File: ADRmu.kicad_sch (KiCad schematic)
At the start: 7 parts, among them J1 DIN41612_02x16_AC_EvenPins, J2 Conn_01x01, J3 Conn_01x01, J4 Conn_01x01, J5 Conn_01x01, J6 Conn_01x01, J7 Conn_01x01

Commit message: asdf
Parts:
- J2: value Conn_01x01 -> 10Vf
- J3: value Conn_01x01 -> 10Vs
- J4: value Conn_01x01 -> ADRf
- J5: value Conn_01x01 -> ADRs
- J6: value Conn_01x01 -> return
- J7: value Conn_01x01 -> guard
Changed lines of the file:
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@@
     (in_bom yes) (on_board yes) (fields_autoplaced)
     (property "Reference" "J4" (id 0) (at 236.22 80.01 0))
-    (property "Value" "Conn_01x01" (id 1) (at 236.22 82.55 0))
+    (property "Value" "ADRf" (id 1) (at 236.22 82.55 0))
     (property "Footprint" "Connector_Wire:SolderWire-1sqmm_1x01_D1.4mm_OD3.9mm" (id 2) (at 236.22 86.36 0)
       (effects (font (size 1.27 1.27)) hide)
@@
     (in_bom yes) (on_board yes) (fields_autoplaced)
     (property "Reference" "J6" (id 0) (at 236.22 110.49 0))
-    (property "Value" "Conn_01x01" (id 1) (at 236.22 113.03 0))
+    (property "Value" "return" (id 1) (at 236.22 113.03 0))
     (property "Footprint" "Connector_Wire:SolderWire-1sqmm_1x01_D1.4mm_OD3.9mm" (id 2) (at 236.22 116.84 0)
       (effects (font (size 1.27 1.27)) hide)
@@
     (in_bom yes) (on_board yes) (fields_autoplaced)
     (property "Reference" "J3" (id 0) (at 236.22 64.77 0))
-    (property "Value" "Conn_01x01" (id 1) (at 236.22 67.31 0))
+    (property "Value" "10Vs" (id 1) (at 236.22 67.31 0))
     (property "Footprint" "Connector_Wire:SolderWire-1sqmm_1x01_D1.4mm_OD3.9mm" (id 2) (at 236.22 71.12 0)
       (effects (font (size 1.27 1.27)) hide)
@@
     (in_bom yes) (on_board yes) (fields_autoplaced)
     (property "Reference" "J5" (id 0) (at 236.22 95.25 0))
-    (property "Value" "Conn_01x01" (id 1) (at 236.22 97.79 0))
+    (property "Value" "ADRs" (id 1) (at 236.22 97.79 0))
     (property "Footprint" "Connector_Wire:SolderWire-1sqmm_1x01_D1.4mm_OD3.9mm" (id 2) (at 236.22 101.6 0)
       (effects (font (size 1.27 1.27)) hide)
@@
     (in_bom yes) (on_board yes)
     (property "Reference" "J2" (id 0) (at 236.22 49.53 0))
-    (property "Value" "Conn_01x01" (id 1) (at 236.22 52.07 0))
+    (property "Value" "10Vf" (id 1) (at 236.22 52.07 0))
     (property "Footprint" "Connector_Wire:SolderWire-1sqmm_1x01_D1.4mm_OD3.9mm" (id 2) (at 236.22 55.88 0)
       (effects (font (size 1.27 1.27)) hide)
@@
     (in_bom yes) (on_board yes) (fields_autoplaced)
     (property "Reference" "J7" (id 0) (at 236.22 125.73 0))
-    (property "Value" "Conn_01x01" (id 1) (at 236.22 128.27 0))
+    (property "Value" "guard" (id 1) (at 236.22 128.27 0))
     (property "Footprint" "Connector_Wire:SolderWire-1sqmm_1x01_D1.4mm_OD3.9mm" (id 2) (at 236.22 132.08 0)
       (effects (font (size 1.27 1.27)) hide)
@@
       (reference "C12") (unit 1) (value "22u") (footprint "Capacitor_SMD:C_1206_3216Metric")
     )
+    (path "/027929a1-62dd-40f4-83d4-39d0de3b1543/6845caeb-6485-48fb-9c50-6cb716fb69d9"
+      (reference "C13") (unit 1) (value "100n") (footprint "Capacitor_SMD:C_0805_2012Metric")
+    )
     (path "/b2eac6f7-6f2b-41aa-9eec-9c2e749d1013/24683382-393e-4151-a76d-4bae24fbeada"
       (reference "C14") (unit 1) (value "100n") (footprint "Capacitor_SMD:C_0805_2012Metric")
@@
       (reference "D7") (unit 1) (value "D_Schottky") (footprint "Diode_SMD:D_SOD-123F")
     )
+    (path "/b2eac6f7-6f2b-41aa-9eec-9c2e749d1013/27618427-173e-42f1-8841-5bc123d4d738"
+      (reference "D8") (unit 1) (value "LED") (footprint "LED_SMD:LED_1206_3216Metric")
+    )
     (path "/b2eac6f7-6f2b-41aa-9eec-9c2e749d1013/8a7e1f15-efce-479e-b3d6-f978918d3a7f"
       (reference "H1") (unit 1) (value "MountingHole") (footprint "MountingHole:MountingHole_4.3mm_M4")
@@
     )
     (path "/adbf8438-12a3-4949-9d6c-a3b68a6378f0"
-      (reference "J2") (unit 1) (value "Conn_01x01") (footprint "Connector_Wire:SolderWire-1sqmm_1x01_D1.4mm_OD3.9mm")
+      (reference "J2") (unit 1) (value "10Vf") (footprint "Connector_Wire:SolderWire-1sqmm_1x01_D1.4mm_OD3.9mm")
     )
     (path "/4bee5892-6b3a-433a-b771-068c80bdc6e8"
-      (reference "J3") (unit 1) (value "Conn_01x01") (footprint "Connector_Wire:SolderWire-1sqmm_1x01_D1.4mm_OD3.9mm")
+      (reference "J3") (unit 1) (value "10Vs") (footprint "Connector_Wire:SolderWire-1sqmm_1x01_D1.4mm_OD3.9mm")
     )
     (path "/27299abf-eabb-45db-a109-6d9800bfa12f"
-      (reference "J4") (unit 1) (value "Conn_01x01") (footprint "Connector_Wire:SolderWire-1sqmm_1x01_D1.4mm_OD3.9mm")
+      (reference "J4") (unit 1) (value "ADRf") (footprint "Connector_Wire:SolderWire-1sqmm_1x01_D1.4mm_OD3.9mm")
     )
     (path "/608a13a4-63e6-4ef1-9c5b-d919cc935a37"
-      (reference "J5") (unit 1) (value "Conn_01x01") (footprint "Connector_Wire:SolderWire-1sqmm_1x01_D1.4mm_OD3.9mm")
+      (reference "J5") (unit 1) (value "ADRs") (footprint "Connector_Wire:SolderWire-1sqmm_1x01_D1.4mm_OD3.9mm")
     )
     (path "/30570277-0b2d-44ac-9416-b1ae1209d471"
-      (reference "J6") (unit 1) (value "Conn_01x01") (footprint "Connector_Wire:SolderWire-1sqmm_1x01_D1.4mm_OD3.9mm")
+      (reference "J6") (unit 1) (value "return") (footprint "Connector_Wire:SolderWire-1sqmm_1x01_D1.4mm_OD3.9mm")
     )
     (path "/e45d5717-29b8-4b31-b3f8-99a046e18c84"
-      (reference "J7") (unit 1) (value "Conn_01x01") (footprint "Connector_Wire:SolderWire-1sqmm_1x01_D1.4mm_OD3.9mm")
+      (reference "J7") (unit 1) (value "guard") (footprint "Connector_Wire:SolderWire-1sqmm_1x01_D1.4mm_OD3.9mm")
     )
     (path "/b2eac6f7-6f2b-41aa-9eec-9c2e749d1013/00d886bb-f578-4690-8703-0d82aa33913b"

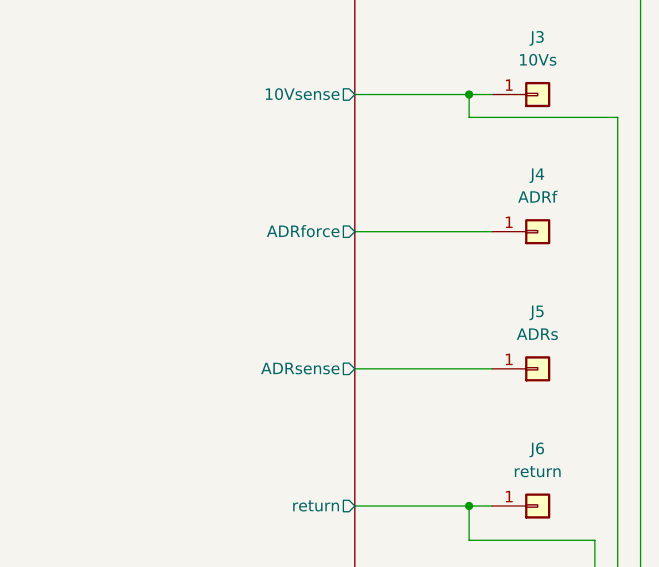
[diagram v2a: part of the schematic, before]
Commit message: added i2c temperature sensor and eeprom
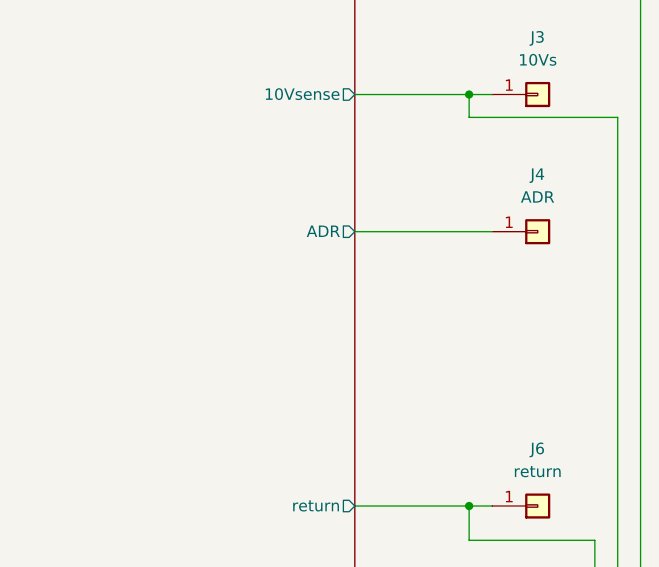
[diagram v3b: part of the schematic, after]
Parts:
- removed J5: ADRs, Connector_Wire:SolderWire-1sqmm_1x01_D1.4mm_OD3.9mm, symbol Connector_Generic:Conn_01x01
- J4: value ADRf -> ADR
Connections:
- net ref/ADRforce renamed ref/ADR
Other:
- sheet ref ports: added ADR; removed ADRforce, ADRsense
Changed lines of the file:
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@@
-    (stroke (width 0) (type default) (color 0 0 0 0))
-  )
-  (wire (pts (xy 215.9 101.6) (xy 231.14 101.6))
     (stroke (width 0) (type default) (color 0 0 0 0))
   )
@@
     (in_bom yes) (on_board yes) (fields_autoplaced)
     (property "Reference" "J4" (id 0) (at 236.22 80.01 0))
-    (property "Value" "ADRf" (id 1) (at 236.22 82.55 0))
+    (property "Value" "ADR" (id 1) (at 236.22 82.55 0))
     (property "Footprint" "Connector_Wire:SolderWire-1sqmm_1x01_D1.4mm_OD3.9mm" (id 2) (at 236.22 86.36 0)
       (effects (font (size 1.27 1.27)) hide)
@@
     )
     (property "Datasheet" "~" (id 3) (at 236.22 71.12 0)
-      (effects (font (size 1.27 1.27)) hide)
-    )
-    (pin "1")
-  )
-  (symbol (lib_id "Connector_Generic:Conn_01x01") (at 236.22 101.6 0) (mirror x) (unit 1)
-    (in_bom yes) (on_board yes) (fields_autoplaced)
-    (property "Reference" "J5" (id 0) (at 236.22 95.25 0))
-    (property "Value" "ADRs" (id 1) (at 236.22 97.79 0))
-    (property "Footprint" "Connector_Wire:SolderWire-1sqmm_1x01_D1.4mm_OD3.9mm" (id 2) (at 236.22 101.6 0)
-      (effects (font (size 1.27 1.27)) hide)
-    )
-    (property "Datasheet" "~" (id 3) (at 236.22 101.6 0)
       (effects (font (size 1.27 1.27)) hide)
     )
@@
       (effects (font (size 1.27 1.27)) (justify right))
     )
-    (pin "ADRsense" output (at 215.9 101.6 0)
-      (effects (font (size 1.27 1.27)) (justify right))
-    )
     (pin "return" output (at 215.9 116.84 0)
       (effects (font (size 1.27 1.27)) (justify right))
     )
-    (pin "ADRforce" output (at 215.9 86.36 0)
-      (effects (font (size 1.27 1.27)) (justify right))
-    )
     (pin "12Vin" input (at 157.48 76.2 180)
       (effects (font (size 1.27 1.27)) (justify left))
@@
     (pin "0Vin" input (at 157.48 111.76 180)
       (effects (font (size 1.27 1.27)) (justify left))
+    )
+    (pin "ADR" output (at 215.9 86.36 0)
+      (effects (font (size 1.27 1.27)) (justify right))
     )
   )
@@
       (reference "#PWR0109") (unit 1) (value "GND") (footprint "")
     )
+    (path "/b2eac6f7-6f2b-41aa-9eec-9c2e749d1013/942f0676-bb26-490c-a5a8-6bd325bcef29"
+      (reference "#PWR0110") (unit 1) (value "GND") (footprint "")
+    )
+    (path "/b2eac6f7-6f2b-41aa-9eec-9c2e749d1013/8855ad76-3b32-484c-b2a9-0614e6f9ce1e"
+      (reference "#PWR0111") (unit 1) (value "+3V3") (footprint "")
+    )
     (path "/b2eac6f7-6f2b-41aa-9eec-9c2e749d1013/8a4e1483-985f-4634-8a4c-4cfa69729777"
       (reference "C1") (unit 1) (value "1000u") (footprint "Capacitor_THT:CP_Radial_D16.0mm_P7.50mm")
@@
       (reference "C15") (unit 1) (value "100n") (footprint "Capacitor_SMD:C_0805_2012Metric")
     )
+    (path "/b2eac6f7-6f2b-41aa-9eec-9c2e749d1013/c7e505b7-3263-497d-b6db-a745ba5df807"
+      (reference "C?") (unit 1) (value "100n") (footprint "Capacitor_SMD:C_0805_2012Metric")
+    )
     (path "/b2eac6f7-6f2b-41aa-9eec-9c2e749d1013/97a99fe4-2863-4a77-a98a-a5b1b9cc3a6a"
       (reference "D1") (unit 1) (value "LED") (footprint "LED_SMD:LED_1206_3216Metric")
@@
     )
     (path "/27299abf-eabb-45db-a109-6d9800bfa12f"
-      (reference "J4") (unit 1) (value "ADRf") (footprint "Connector_Wire:SolderWire-1sqmm_1x01_D1.4mm_OD3.9mm")
-    )
-    (path "/608a13a4-63e6-4ef1-9c5b-d919cc935a37"
-      (reference "J5") (unit 1) (value "ADRs") (footprint "Connector_Wire:SolderWire-1sqmm_1x01_D1.4mm_OD3.9mm")
+      (reference "J4") (unit 1) (value "ADR") (footprint "Connector_Wire:SolderWire-1sqmm_1x01_D1.4mm_OD3.9mm")
     )
     (path "/30570277-0b2d-44ac-9416-b1ae1209d471"
@@
       (reference "U6") (unit 1) (value "LT3045xMSE") (footprint "Package_SO:MSOP-12-1EP_3x4mm_P0.65mm_EP1.65x2.85mm")
     )
-  )
+    (path "/b2eac6f7-6f2b-41aa-9eec-9c2e749d1013/018002e6-06ae-46c7-887f-c27f45825467"
+      (reference "U7") (unit 1) (value "24AA02-OT") (footprint "Package_TO_SOT_SMD:SOT-23-5")
+    )
+  )

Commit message: asas
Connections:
- net DC-DC/Vin-: now also J1.a16 (Pin_a16), J1.c16 (Pin_c16)
- net DC-DC/status: now reaches J1.a14 (Pin_a14)
- net DC-DC/status: now also J1.c14 (Pin_c14)
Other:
- sheet DC-DC ports: added status; removed none
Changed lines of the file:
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@@
   (junction (at 68.58 82.55) (diameter 0) (color 0 0 0 0)
   )
+  (junction (at 55.88 92.71) (diameter 0) (color 0 0 0 0)
+  )
   (junction (at 55.88 100.33) (diameter 0) (color 0 0 0 0)
   )
@@
   (junction (at 68.58 105.41) (diameter 0) (color 0 0 0 0)
   )
+  (junction (at 68.58 90.17) (diameter 0) (color 0 0 0 0)
+  )
   (junction (at 68.58 85.09) (diameter 0) (color 0 0 0 0)
   )
   (junction (at 68.58 113.03) (diameter 0) (color 0 0 0 0)
   )
+  (junction (at 52.07 92.71) (diameter 0) (color 0 0 0 0)
+  )
   (junction (at 68.58 110.49) (diameter 0) (color 0 0 0 0)
   )
@@
     (stroke (width 0) (type default) (color 0 0 0 0))
   )
+  (wire (pts (xy 55.88 92.71) (xy 68.58 92.71))
+    (stroke (width 0) (type default) (color 0 0 0 0))
+  )
   (wire (pts (xy 228.6 120.65) (xy 228.6 116.84))
     (stroke (width 0) (type default) (color 0 0 0 0))
@@
     (stroke (width 0) (type default) (color 0 0 0 0))
   )
+  (wire (pts (xy 55.88 90.17) (xy 68.58 90.17))
+    (stroke (width 0) (type default) (color 0 0 0 0))
+  )
   (wire (pts (xy 55.88 77.47) (xy 52.07 77.47))
     (stroke (width 0) (type default) (color 0 0 0 0))
   )
+  (wire (pts (xy 68.58 90.17) (xy 83.82 90.17))
+    (stroke (width 0) (type default) (color 0 0 0 0))
+  )
   (wire (pts (xy 68.58 74.93) (xy 83.82 74.93))
     (stroke (width 0) (type default) (color 0 0 0 0))
@@
     (stroke (width 0) (type default) (color 0 0 0 0))
   )
+  (wire (pts (xy 52.07 92.71) (xy 52.07 100.33))
+    (stroke (width 0) (type default) (color 0 0 0 0))
+  )
   (wire (pts (xy 231.14 116.84) (xy 228.6 116.84))
     (stroke (width 0) (type default) (color 0 0 0 0))
@@
     (stroke (width 0) (type default) (color 0 0 0 0))
   )
+  (wire (pts (xy 52.07 92.71) (xy 55.88 92.71))
+    (stroke (width 0) (type default) (color 0 0 0 0))
+  )
   (wire (pts (xy 245.11 73.66) (xy 245.11 156.21))
     (stroke (width 0) (type default) (color 0 0 0 0))
@@
     (stroke (width 0) (type default) (color 0 0 0 0))
   )
-  (wire (pts (xy 52.07 87.63) (xy 52.07 100.33))
+  (wire (pts (xy 52.07 87.63) (xy 52.07 92.71))
     (stroke (width 0) (type default) (color 0 0 0 0))
   )
@@
       (effects (font (size 1.27 1.27)) (justify left))
     )
+    (pin "status" input (at 83.82 90.17 180)
+      (effects (font (size 1.27 1.27)) (justify left))
+    )
   )
   (sheet_instances
@@
     )
     (path "/b2eac6f7-6f2b-41aa-9eec-9c2e749d1013/c7e505b7-3263-497d-b6db-a745ba5df807"
-      (reference "C?") (unit 1) (value "100n") (footprint "Capacitor_SMD:C_0805_2012Metric")
+      (reference "C16") (unit 1) (value "100n") (footprint "Capacitor_SMD:C_0805_2012Metric")
+    )
+    (path "/b2eac6f7-6f2b-41aa-9eec-9c2e749d1013/f4163a13-75d2-44f7-a286-ce9ec4db0e92"
+      (reference "C17") (unit 1) (value "22u") (footprint "Capacitor_SMD:C_1206_3216Metric")
     )
     (path "/b2eac6f7-6f2b-41aa-9eec-9c2e749d1013/97a99fe4-2863-4a77-a98a-a5b1b9cc3a6a"
@@
       (reference "Q1") (unit 1) (value "Q_NPN_BCE") (footprint "Package_TO_SOT_SMD:SOT-223-3_TabPin2")
     )
+    (path "/b2eac6f7-6f2b-41aa-9eec-9c2e749d1013/1013018f-229b-406c-9517-97d026acdb9a"
+      (reference "Q2") (unit 1) (value "MMBT3904") (footprint "Package_TO_SOT_SMD:SOT-23")
+    )
     (path "/b2eac6f7-6f2b-41aa-9eec-9c2e749d1013/cf8213e3-6210-4f84-8e3b-63bd409ba25a"
       (reference "R1") (unit 1) (value "5k") (footprint "Resistor_SMD:R_0805_2012Metric")
@@
       (reference "R12") (unit 1) (value "121k") (footprint "Resistor_SMD:R_0805_2012Metric")
     )
+    (path "/027929a1-62dd-40f4-83d4-39d0de3b1543/36ed9d27-6de2-4596-b802-4666aa392e35"
+      (reference "R13") (unit 1) (value "dnp") (footprint "Resistor_SMD:R_0805_2012Metric")
+    )
+    (path "/027929a1-62dd-40f4-83d4-39d0de3b1543/e22465b8-acc1-46c4-9b5d-e2e4156397d5"
+      (reference "R14") (unit 1) (value "dnp") (footprint "Crystal:Crystal_HC52-U_Vertical")
+    )
+    (path "/027929a1-62dd-40f4-83d4-39d0de3b1543/194203bb-0c5b-44d0-b461-32ccc04431bc"
+      (reference "R15") (unit 1) (value "0") (footprint "Resistor_SMD:R_0805_2012Metric")
+    )
+    (path "/027929a1-62dd-40f4-83d4-39d0de3b1543/53cee888-d3e3-4eb2-94ea-0265cbb211bf"
+      (reference "R16") (unit 1) (value "0") (footprint "Crystal:Crystal_HC52-U_Vertical")
+    )
+    (path "/027929a1-62dd-40f4-83d4-39d0de3b1543/dfc35787-ea86-4988-ae38-87f6d9a08516"
+      (reference "R17") (unit 1) (value "0") (footprint "Resistor_SMD:R_0805_2012Metric")
+    )
+    (path "/027929a1-62dd-40f4-83d4-39d0de3b1543/15dd7c7a-30db-4890-a373-61f9b60fae6f"
+      (reference "R18") (unit 1) (value "0") (footprint "Crystal:Crystal_HC52-U_Vertical")
+    )
+    (path "/b2eac6f7-6f2b-41aa-9eec-9c2e749d1013/b6374ec4-7ed7-459e-befd-2e08e8f885b1"
+      (reference "R19") (unit 1) (value "5k") (footprint "Resistor_SMD:R_0805_2012Metric")
+    )
+    (path "/b2eac6f7-6f2b-41aa-9eec-9c2e749d1013/c704b6f6-f527-4c2e-9d83-ff759777f370"
+      (reference "R20") (unit 1) (value "200k") (footprint "Resistor_SMD:R_0805_2012Metric")
+    )
+    (path "/b2eac6f7-6f2b-41aa-9eec-9c2e749d1013/cdb664ee-3f00-4c5a-af63-9c9dadcc63d1"
+      (reference "R21") (unit 1) (value "1.8M") (footprint "Resistor_SMD:R_0805_2012Metric")
+    )
+    (path "/b2eac6f7-6f2b-41aa-9eec-9c2e749d1013/590dbea1-342c-423f-9920-ea67e378a0c1"
+      (reference "R22") (unit 1) (value "49.9k") (footprint "Resistor_SMD:R_0805_2012Metric")
+    )
     (path "/027929a1-62dd-40f4-83d4-39d0de3b1543/61e33ddb-fb2f-4483-96fd-ca725420cb1a"
